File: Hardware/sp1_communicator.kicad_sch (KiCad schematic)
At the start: 0 parts

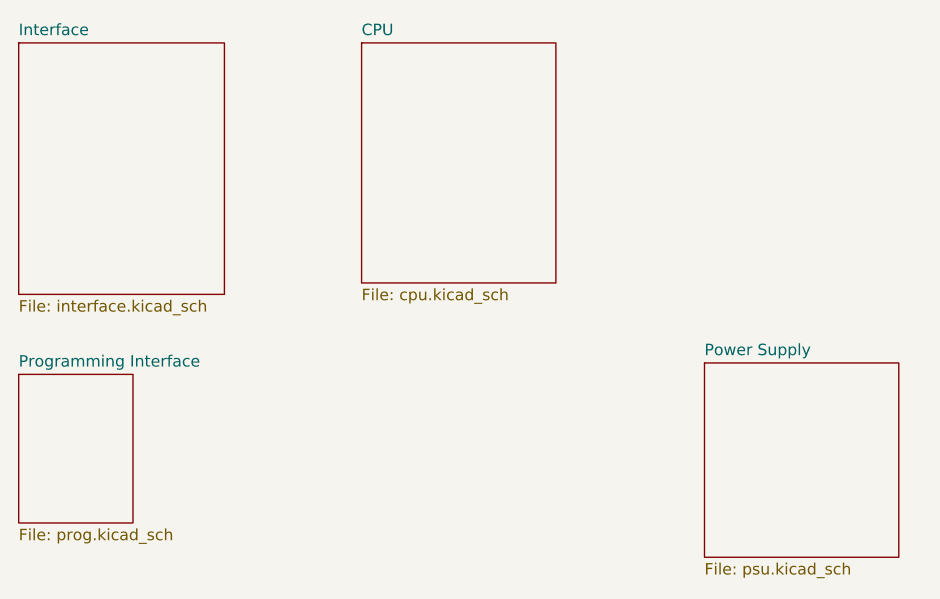
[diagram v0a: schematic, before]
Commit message: Rebuild p1_reader project
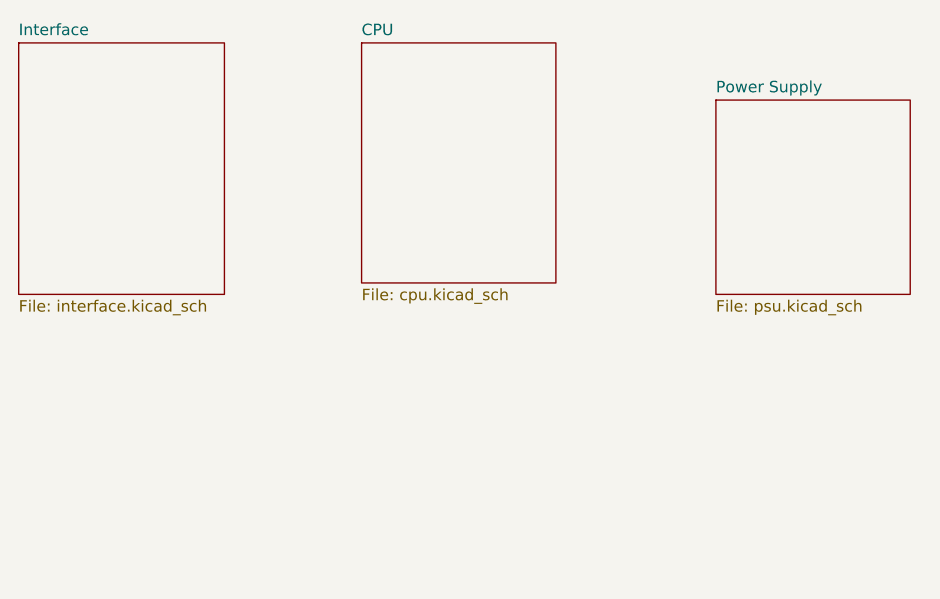
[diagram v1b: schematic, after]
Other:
- removed sheet Programming Interface
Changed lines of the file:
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@@
-(kicad_sch (version 20211123) (generator eeschema)
+(kicad_sch (version 20230121) (generator eeschema)
   (paper "A4")
   (title_block
@@
   )
   (sheet (at 124.46 45.72) (size 21.59 26.67) (fields_autoplaced)
-    (stroke (width 0.1524) (type solid) (color 0 0 0 0))
+    (stroke (width 0.1524) (type solid))
     (fill (color 0 0 0 0.0000))
-    (property "Sheet name" "CPU" (id 0) (at 124.46 45.0084 0)
+    (property "Sheetname" "CPU" (at 124.46 45.0084 0)
       (effects (font (size 1.27 1.27)) (justify left bottom))
     )
-    (property "Sheet file" "cpu.kicad_sch" (id 1) (at 124.46 72.9746 0)
+    (property "Sheetfile" "cpu.kicad_sch" (at 124.46 72.9746 0)
       (effects (font (size 1.27 1.27)) (justify left top))
     )
+    (instances
+      (project "sp1_communicator"
+        (path "/d9bd008b-84e8-4d0b-9177-df1b9a254894" (page "2"))
+      )
+    )
   )
-  (sheet (at 162.56 81.28) (size 21.59 21.59) (fields_autoplaced)
-    (stroke (width 0.1524) (type solid) (color 0 0 0 0))
+  (sheet (at 163.83 52.07) (size 21.59 21.59) (fields_autoplaced)
+    (stroke (width 0.1524) (type solid))
     (fill (color 0 0 0 0.0000))
-    (property "Sheet name" "Power Supply" (id 0) (at 162.56 80.5684 0)
+    (property "Sheetname" "Power Supply" (at 163.83 51.3584 0)
       (effects (font (size 1.27 1.27)) (justify left bottom))
     )
-    (property "Sheet file" "psu.kicad_sch" (id 1) (at 162.56 103.4546 0)
+    (property "Sheetfile" "psu.kicad_sch" (at 163.83 74.2446 0)
       (effects (font (size 1.27 1.27)) (justify left top))
+    )
+    (instances
+      (project "sp1_communicator"
+        (path "/d9bd008b-84e8-4d0b-9177-df1b9a254894" (page "4"))
+      )
     )
   )
   (sheet (at 86.36 45.72) (size 22.86 27.94) (fields_autoplaced)
-    (stroke (width 0.1524) (type solid) (color 0 0 0 0))
+    (stroke (width 0.1524) (type solid))
     (fill (color 0 0 0 0.0000))
-    (property "Sheet name" "Interface" (id 0) (at 86.36 45.0084 0)
+    (property "Sheetname" "Interface" (at 86.36 45.0084 0)
       (effects (font (size 1.27 1.27)) (justify left bottom))
     )
-    (property "Sheet file" "interface.kicad_sch" (id 1) (at 86.36 74.2446 0)
+    (property "Sheetfile" "interface.kicad_sch" (at 86.36 74.2446 0)
       (effects (font (size 1.27 1.27)) (justify left top))
     )
-  )
-  (sheet (at 86.36 82.55) (size 12.7 16.51) (fields_autoplaced)
-    (stroke (width 0.1524) (type solid) (color 0 0 0 0))
-    (fill (color 0 0 0 0.0000))
-    (property "Sheet name" "Programming Interface" (id 0) (at 86.36 81.8384 0)
-      (effects (font (size 1.27 1.27)) (justify left bottom))
-    )
-    (property "Sheet file" "prog.kicad_sch" (id 1) (at 86.36 99.6446 0)
-      (effects (font (size 1.27 1.27)) (justify left top))
+    (instances
+      (project "sp1_communicator"
+        (path "/d9bd008b-84e8-4d0b-9177-df1b9a254894" (page "3"))
+      )
     )
   )
   (sheet_instances
     (path "/" (page "1"))
-    (path "/09d88c85-f555-474c-9d74-2222a962560f" (page "2"))
-    (path "/7d5948d1-8ff5-41bc-bc50-eec041142a58" (page "3"))
-    (path "/1a25c7cc-42d7-46c2-b12d-34ac8b0e855a" (page "4"))
-    (path "/f3cb2ff7-19d1-4894-834e-ceb1f696009b" (page "5"))
-  )
-  (symbol_instances
-    (path "/7d5948d1-8ff5-41bc-bc50-eec041142a58/1cd3f03c-67e0-4ed1-8032-ccc9eac5065e"
-      (reference "#PWR?") (unit 1) (value "+5V") (footprint "")
-    )
-    (path "/7d5948d1-8ff5-41bc-bc50-eec041142a58/9f724fce-ef64-47d0-a16a-353718e79e18"
-      (reference "#PWR?") (unit 1) (value "GND") (footprint "")
-    )
-    (path "/7d5948d1-8ff5-41bc-bc50-eec041142a58/3deb6feb-41a4-4570-81d0-cd4de5221f52"
-      (reference "J?") (unit 1) (value "CRJ030-G-TH") (footprint "CUI_CRJ030-G-TH")
-    )
   )
 )

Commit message: Resumed schematic
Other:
- sheet CPU ports: added DATA, RQ; removed none
- sheet Interface ports: added DATA, RQ; removed none
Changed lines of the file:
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@@
     (company "Manul Technologies")
   )
-  (sheet (at 124.46 45.72) (size 21.59 26.67) (fields_autoplaced)
+  (wire (pts (xy 109.22 47.625) (xy 121.285 47.625))
+    (stroke (width 0) (type default))
+  )
+  (wire (pts (xy 109.22 50.165) (xy 121.285 50.165))
+    (stroke (width 0) (type default))
+  )
+  (sheet (at 121.285 45.72) (size 12.7 6.35) (fields_autoplaced)
     (stroke (width 0.1524) (type solid))
     (fill (color 0 0 0 0.0000))
-    (property "Sheetname" "CPU" (at 124.46 45.0084 0)
+    (property "Sheetname" "CPU" (at 121.285 45.0084 0)
       (effects (font (size 1.27 1.27)) (justify left bottom))
     )
-    (property "Sheetfile" "cpu.kicad_sch" (at 124.46 72.9746 0)
+    (property "Sheetfile" "cpu.kicad_sch" (at 121.285 52.6546 0)
       (effects (font (size 1.27 1.27)) (justify left top))
+    )
+    (pin "DATA" input (at 121.285 47.625 180)
+      (effects (font (size 1.27 1.27)) (justify left))
+    )
+    (pin "RQ" output (at 121.285 50.165 180)
+      (effects (font (size 1.27 1.27)) (justify left))
     )
     (instances
@@
     )
   )
-  (sheet (at 163.83 52.07) (size 21.59 21.59) (fields_autoplaced)
+  (sheet (at 77.47 45.72) (size 12.7 6.35) (fields_autoplaced)
     (stroke (width 0.1524) (type solid))
     (fill (color 0 0 0 0.0000))
-    (property "Sheetname" "Power Supply" (at 163.83 51.3584 0)
+    (property "Sheetname" "Power Supply" (at 77.47 45.0084 0)
       (effects (font (size 1.27 1.27)) (justify left bottom))
     )
-    (property "Sheetfile" "psu.kicad_sch" (at 163.83 74.2446 0)
+    (property "Sheetfile" "psu.kicad_sch" (at 77.47 52.6546 0)
       (effects (font (size 1.27 1.27)) (justify left top))
     )
@@
     )
   )
-  (sheet (at 86.36 45.72) (size 22.86 27.94) (fields_autoplaced)
+  (sheet (at 96.52 45.72) (size 12.7 6.35) (fields_autoplaced)
     (stroke (width 0.1524) (type solid))
     (fill (color 0 0 0 0.0000))
-    (property "Sheetname" "Interface" (at 86.36 45.0084 0)
+    (property "Sheetname" "Interface" (at 96.52 45.0084 0)
       (effects (font (size 1.27 1.27)) (justify left bottom))
     )
-    (property "Sheetfile" "interface.kicad_sch" (at 86.36 74.2446 0)
+    (property "Sheetfile" "interface.kicad_sch" (at 96.52 52.6546 0)
       (effects (font (size 1.27 1.27)) (justify left top))
     )
+    (pin "RQ" input (at 109.22 50.165 0)
+      (effects (font (size 1.27 1.27)) (justify right))
+    )
+    (pin "DATA" output (at 109.22 47.625 0)
+      (effects (font (size 1.27 1.27)) (justify right))
+    )
     (instances

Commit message: completed routing
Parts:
- added C1, C3: 10uF, Capacitor_SMD:C_0402_1005Metric, symbol Device:C_Small
- added C10, C11: TBD, Capacitor_SMD:C_0402_1005Metric, symbol Device:C_Small
- added C2, C8, C9: 100nF, Capacitor_SMD:C_0402_1005Metric, symbol Device:C_Small
- added C4, C5: 10uF, Capacitor_SMD:CP_Elec_6.3x5.7, symbol Device:C_Polarized_Small
- added C6, C7: 22uF, Capacitor_SMD:C_1210_3225Metric, symbol Device:C_Small
- added D1: 82400102, Package_TO_SOT_SMD:SOT-23-6, symbol manul_tech:82400102
- added D2, D3: 1N5819W, Diode_SMD:D_SOD-123, symbol manul_tech:1N5819W
- added J1: 615006138421, manul_tech:615006138421, symbol manul_tech:615006138421
- added J2: 629722000214, manul_tech:629722000214, symbol manul_tech:629722000214
- added L1: 1uH, Inductor_SMD:L_Wuerth_WE-PD2-Typ-MS, symbol Device:L_Small
- added R1, R12, R4, R8, R9: 10K, Resistor_SMD:R_0402_1005Metric, symbol Device:R_Small
- added R10, R11, R5: 220R, Resistor_SMD:R_0402_1005Metric, symbol Device:R_Small
- added R13, R14: 0R, Resistor_SMD:R_0402_1005Metric, symbol Device:R_Small
- added R2: 1M, Resistor_SMD:R_0402_1005Metric, symbol Device:R_Small
- added R3: 1K, Resistor_SMD:R_0402_1005Metric, symbol Device:R_Small
- added R6, R7: 5.1K, Resistor_SMD:R_0402_1005Metric, symbol Device:R_Small
- added SW1, SW2: KSEM31JLFS, manul_tech:KSEM31JLFS, symbol manul_tech:KSEM31JLFS
- added U1, U2: 140357145100, Package_SO:SOP-4_3.8x4.1mm_P2.54mm, symbol manul_tech:140357145100
- added U3: 173950336, manul_tech:SIP3_11.6x8.5mm, symbol manul_tech:173950336
- added U4: ESP32-C3-WROOM-02U-N4, manul_tech:MODULE_ESP32-C3-WROOM-02-H4, symbol manul_tech:ESP32-C3-WROOM-02-N4
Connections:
- new net: R12.2, U4.16 (IO2)
- new net: C4.1, D2.1 (K), D3.1 (K), L1.1
- new net: C5.1, L1.2, U3.1 (VIN)
- new net: J2.B5 (CC2), R7.1
- new net: J2.A5 (CC1), R6.2
- new net: C10.1, D1.6 (IO1), R13.1
- new net: C11.1, D1.4 (IO2), R14.1
- new net: R10.1, SW1.3
- new net: R3.2, U2.1
- new net: R1.2, U1.4
- new net: R11.1, SW2.3
- new net: R5.2, U1.1
- new net +3V3: C2.1, C3.1, C6.1, C7.1, R12.1, R4.1, R8.1, R9.1, U3.3 (VOUT), U4.1 (3V3)
- new net +5V: D2.2 (A), J1.1, R1.1, R3.1
- new net BOOT: C8.2, R9.2, SW2.1, U4.8 (IO9)
- new net D+: D1.1 (IO1), J2.A6 (D+1), J2.B6 (D+2)
- new net D-: D1.3 (IO2), J2.A7 (D-1), J2.B7 (D-2)
- new net DA+: R13.2, U4.14 (IO19)
- new net DA-: R14.2, U4.13 (IO18)
- new net EN: C1.1, C9.2, R8.2, SW1.1, U4.2 (EN)
- new net GND: C1.2, C10.2, C11.2, C2.2, C3.2, C4.2, C5.2, C6.2, C7.2, C8.1, C9.1, D1.2 (GND), J1.3, J1.6, J2.A1 (GND), J2.A12 (GND), J2.S1 (SHIELD), J2.S2 (SHIELD), J2.S3 (SHIELD), J2.S4 (SHIELD), R10.2, R11.2, R2.2, R6.1, R7.2, U1.2, U2.3, U3.2 (GND), U4.19_1 (GND), U4.19_2 (GND), U4.19_3 (GND), U4.19_4 (GND), U4.19_5 (GND), U4.19_6 (GND), U4.19_7 (GND), U4.19_8 (GND), U4.19_9 (GND), U4.9 (GND)
- new net REQ: J1.2, R2.1, U1.3
- new net RTS: R5.1, U4.4 (IO5)
- new net RX: R4.2, U2.4, U4.5 (IO6)
- new net VBUS: D1.5 (VDD), D3.2 (A), J2.A4 (VBUS), J2.A9 (VBUS)
- new net ~{DATA}: J1.5, U2.2
- no-connect marks 0 -> 14
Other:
- removed sheet CPU
- removed sheet Interface
- removed sheet Power Supply
- note added: "BOOT MODE & RESET BUTTONS"
- note added: "DC/DC Power Supply"
- note added: "MCU (ESP32-C3)"
- note added: "P1 Interface (RJ11)"
- note added: "USB-C AND ESD PROTECTION"
- title: Standalone P1 Protocol Reader -> P1 Wireless Interface

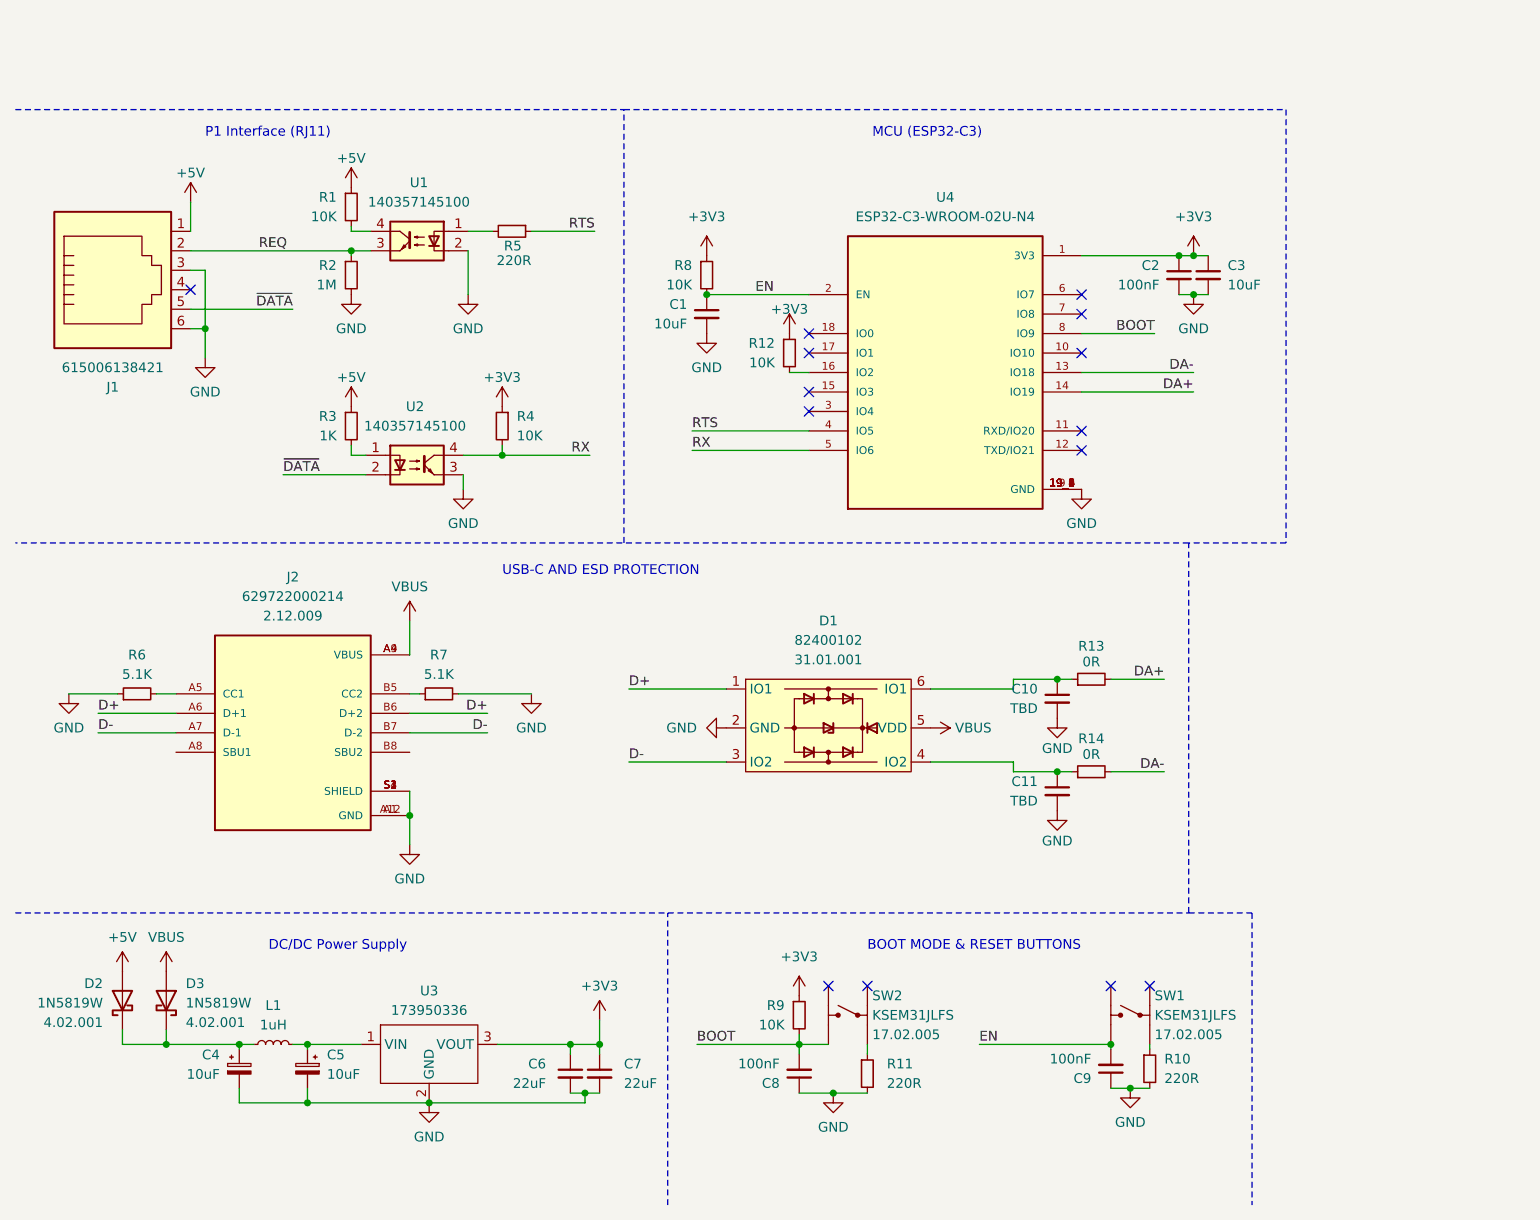
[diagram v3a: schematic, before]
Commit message: Added status led and power led and mounting holes
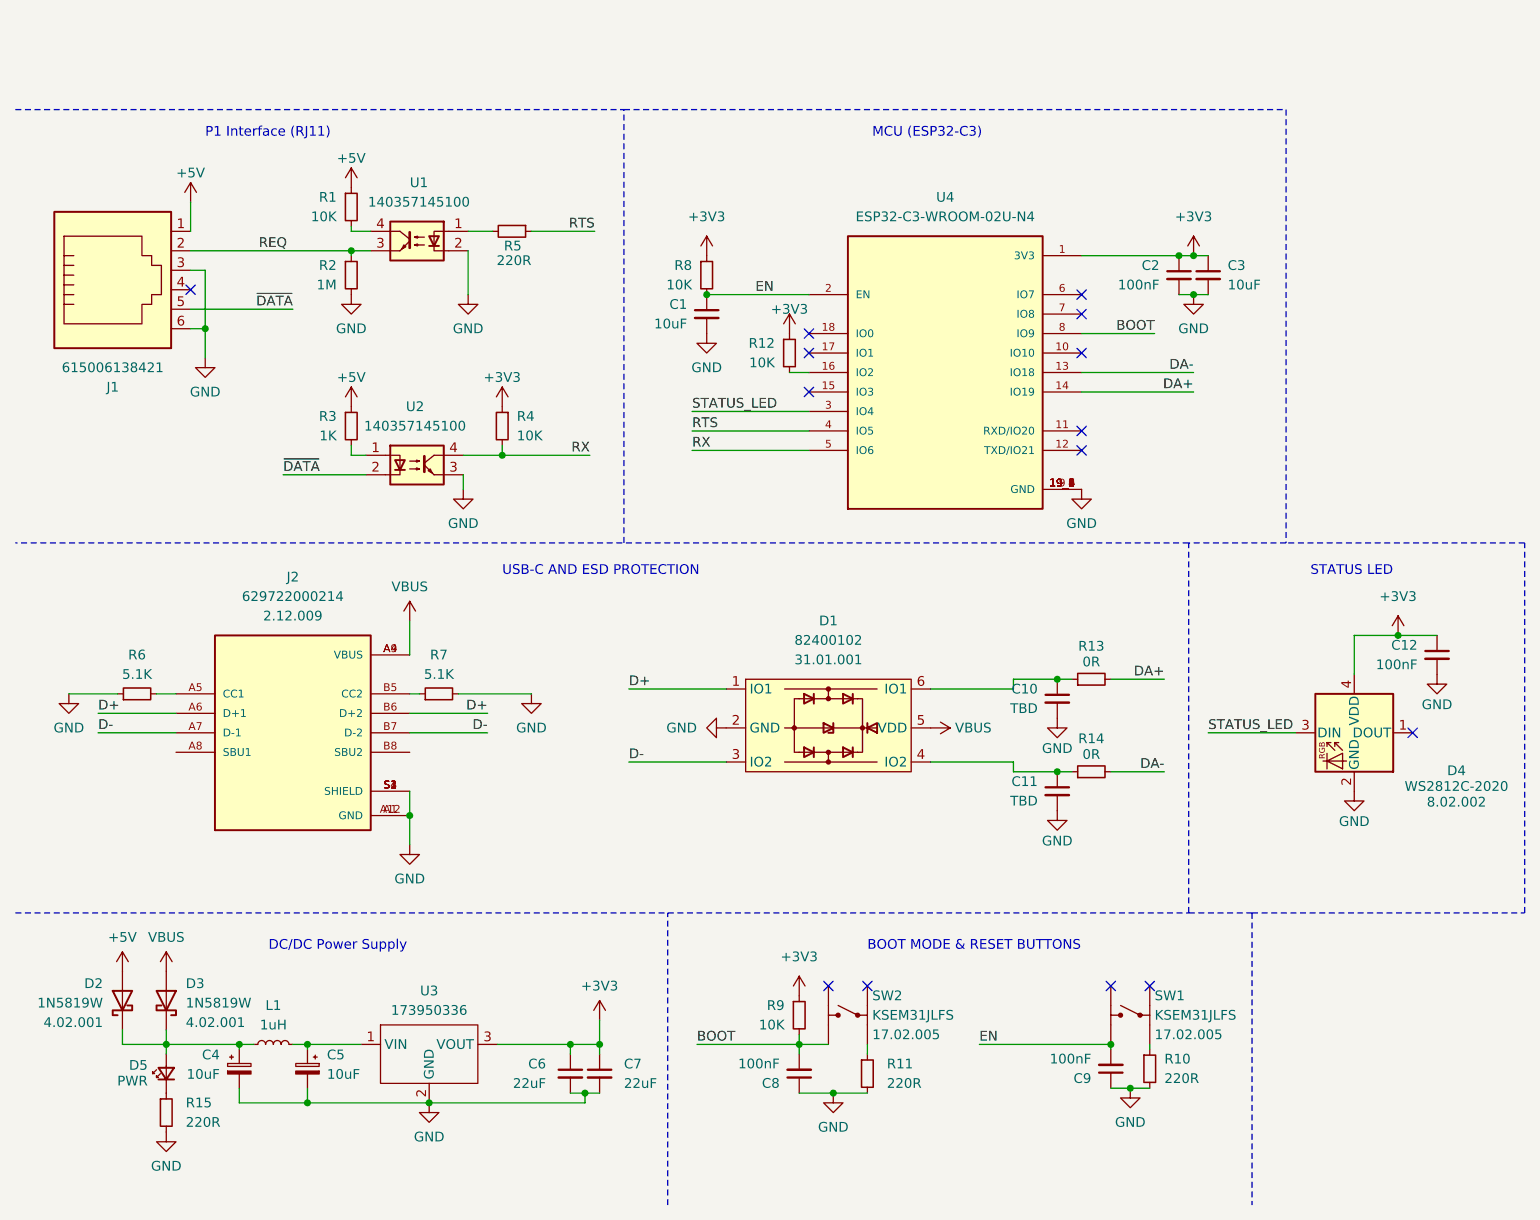
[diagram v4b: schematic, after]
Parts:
- added C12: 100nF, Capacitor_SMD:C_0402_1005Metric, symbol Device:C_Small
- added D4: WS2812C-2020, manul_tech:LED_WS2812C-2020, symbol manul_tech:WS2812C-2020
- added D5: PWR, LED_SMD:LED_0402_1005Metric, symbol Device:LED_Small
- added R15: 220R, Resistor_SMD:R_0402_1005Metric, symbol Device:R_Small
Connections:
- net +3V3: now also C12.1, D4.4 (VDD)
- net GND: now also C12.2, D4.2 (GND), R15.2
- net at C4.1, D2.1 (K), D3.1 (K)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: now also D5.2 (A)
- net STATUS_LED: now reaches U4.3 (IO4)
- net STATUS_LED: now also D4.3 (DIN)
- new net: D5.1 (K), R15.1
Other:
- note added: "STATUS LED"
